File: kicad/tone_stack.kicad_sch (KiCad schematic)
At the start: 4 parts

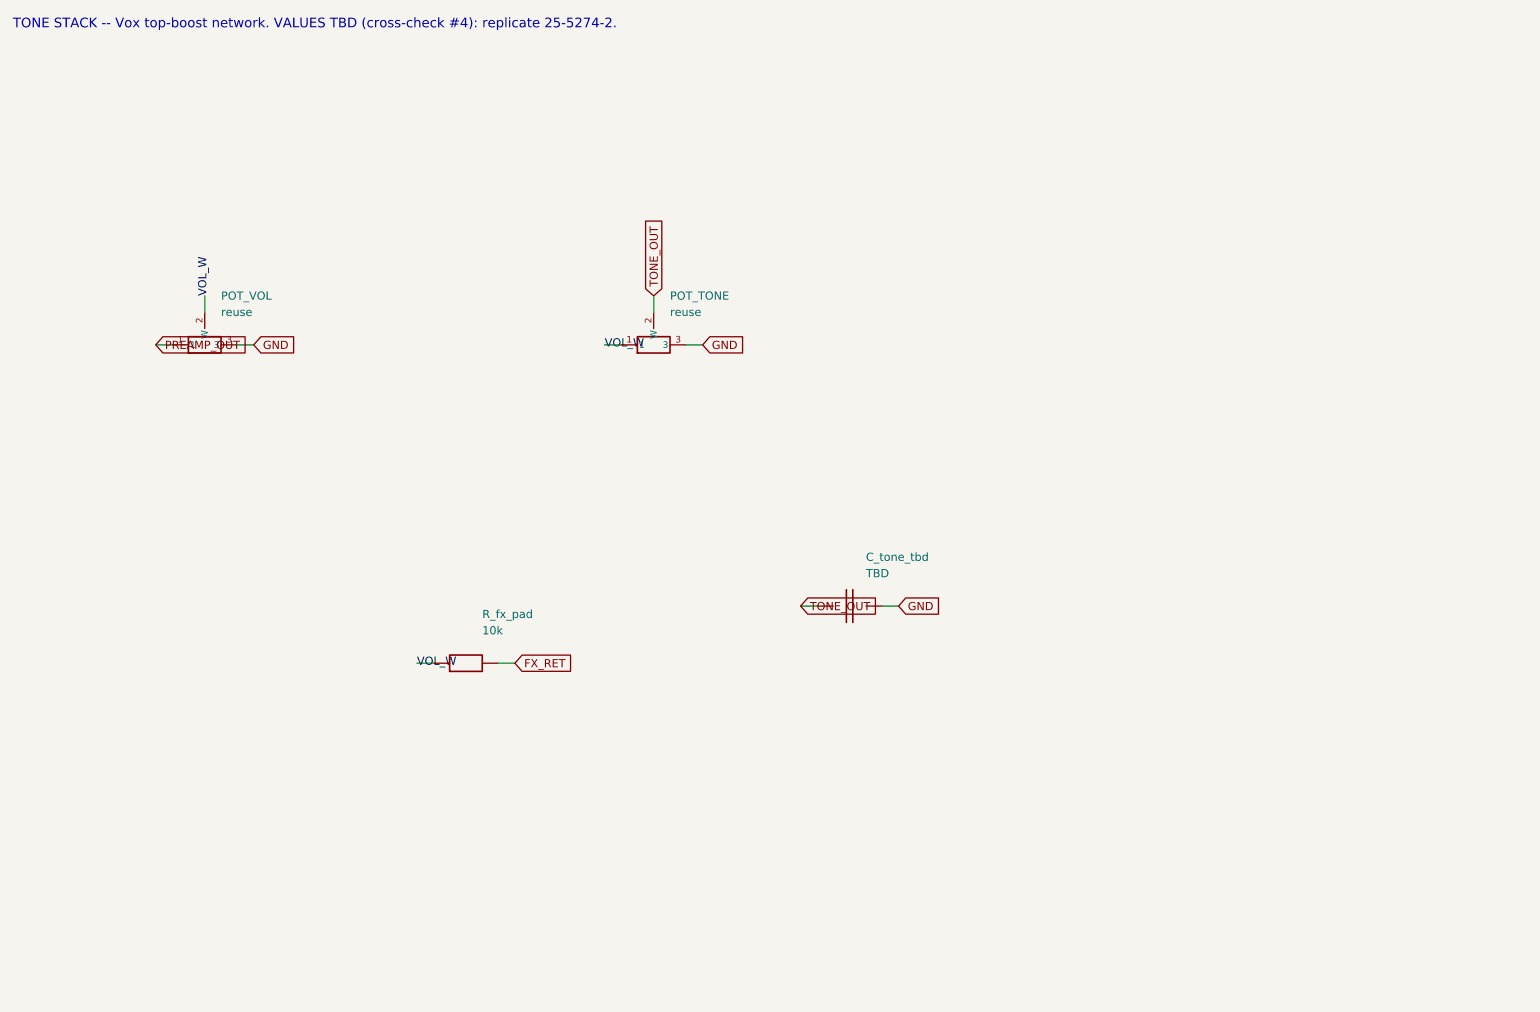
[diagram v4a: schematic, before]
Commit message: Audit pass: center schematic pages, PCB layout audit, SPICE audit
Schematic: gen_kicad.py now defers draw-op emission, computes each sheet's
content bounding box, and translates it to the page center (grid-snapped so pins
stay on the 1.27mm grid). All 8 sheets are centered on the page instead of
crammed top-left; ERC still 0 violations.

PCB: full category-by-category audit in kicad/PCB-AUDIT.md (footprints,
placement, net classes, copper/GND, routing) with prioritized fixes. Applied:
- the 5 reused/off-board pots were modeled with a 16mm panel-pot footprint; they
  are panel-mounted (wired off-board), so they're now 3-pad wiring connectors --
  more correct and a big silk-overlap source removed (packing 51%->48%)
- centered the component grid
Documented findings: LM1875 TO-220-5 annular is 0.0875mm (1.275mm pad on 1.1mm
drill) vs the 0.15mm rule; KBP410G bridge uses a placeholder header footprint;
silk/courtyard overlaps are a density symptom (the 82% packing on the 155x90
safe-bet). Non-routing DRC errors: 9; demo board still 0.

SPICE: audited every netlist/model (spice/README.md). All five run under
ngspice-42 (exit 0) and match the documented numbers; no correctness issues.

https://claude.ai/code/session_01PkrfUi9tvZfLvudJ7h23qD
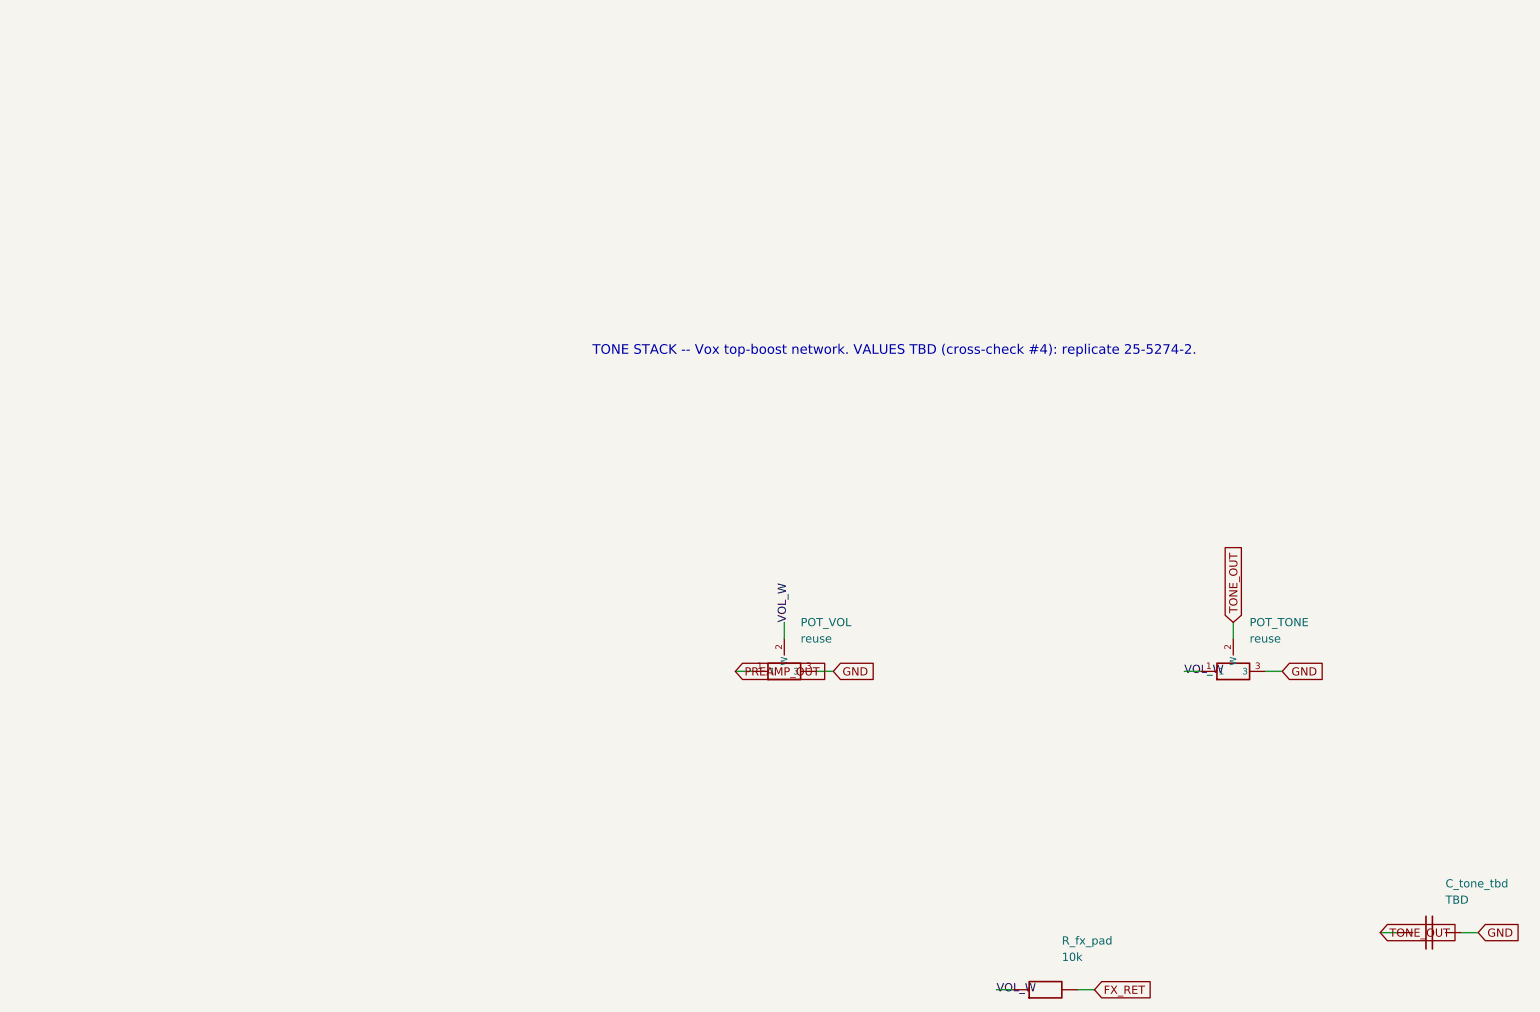
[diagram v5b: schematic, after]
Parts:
- POT_TONE, POT_VOL: footprint Potentiometer_THT:Potentiometer_Alpha_RD901F-40-00D_Single_Vertical -> Connector_PinHeader_2.54mm:PinHeader_1x03_P2.54mm_Vertical
